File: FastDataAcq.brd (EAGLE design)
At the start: 114.3 x 63.2 mm, 223 parts, among them IC1 LT1963AEQ, IC2 FT230XQ, IC3 ADCMP553BRMZ, J1 MICRO-FIT_3.0_2POS_RA_SMD, J2 USB_MICROAB_SMT, J3 HEADER_0.1"_10P_2R_SMT, X1 87832-14, X2 SMA-142-0701-801/806, X3 SMA-142-0701-801/806, Y1 SI530-500, Y2 100MHz, Y3 DNP

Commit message: Digital layout complete.
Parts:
- moved TP13 25.2 mm to (76.4, 84.2)
- moved D2 17.0 mm to (106.7, 69.3), turned to 0 degrees
- moved R42 17.0 mm to (104.6, 69.3), flipped to the bottom, turned to 180 degrees
- moved D3 16.8 mm to (106.7, 67.8), turned to 0 degrees
- moved R43 16.8 mm to (104.6, 67.8), flipped to the bottom, turned to 180 degrees
- moved D4 11.7 mm to (106.7, 70.9), turned to 0 degrees
- moved R44 11.7 mm to (104.6, 70.9), flipped to the bottom, turned to 180 degrees
- moved J3 0.57 mm to (98.6, 73.4)
- moved Y3 0.28 mm to (84.3, 53.0)
- moved C85 0.25 mm to (88.4, 52.1)
- moved C86 0.25 mm to (87.4, 52.1)
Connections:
- removed net N3: U$2.P$62
- removed net N4: U$2.P$61
- removed net N5: U$2.P$59
- removed net N6: U$2.P$58
- removed net N7: U$2.P$57
- removed net N8: U$2.P$48
- removed net N9: U$2.P$47
- net 3V3: now also J3.P$9; no longer J3.P$1
- net FPGA_GPIO1: now also J3.P$4, U$2.P$47; no longer J3.P$9
- net FPGA_GPIO2: now also J3.P$2, U$2.P$48; no longer J3.P$8
- net FPGA_GPIO3: now also J3.P$1, U$2.P$57; no longer J3.P$7
- net FPGA_GPIO4: now also D3.CATHODE, J3.P$7, U$2.P$58; no longer J3.P$6
- net FPGA_GPIO5: now also J3.P$6, U$2.P$59; no longer J3.P$5
- net FPGA_GPIO6: now also D2.CATHODE, J3.P$5, U$2.P$61; no longer D3.CATHODE, J3.P$4
- net FPGA_GPIO7: now also U$2.P$62; no longer D2.CATHODE
- net GND: now also J3.P$10; no longer J3.P$2
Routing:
- net FPGA_GPIO1: track 0.00 -> 59.0 mm, vias 0 -> 2
- net FPGA_GPIO5: track 0.00 -> 57.6 mm, vias 0 -> 7
- net FPGA_GPIO2: track 0.00 -> 51.6 mm, vias 0 -> 2
- net FPGA_GPIO4: track 0.00 -> 48.7 mm, vias 0 -> 2
- net FPGA_GPIO6: track 0.00 -> 48.6 mm, vias 0 -> 4
- net FPGA_GPIO3: track 0.00 -> 42.2 mm, vias 0 -> 2
- net FPGA_GPIO7: track 0.00 -> 38.0 mm, vias 0 -> 2
- net 3V3: track 51.8 -> 83.8 mm, vias 27 -> 30
- net FPGA_TCK: track 38.4 -> 49.1 mm, vias 3 -> 4
- net FPGA_TMS: track 32.9 -> 42.8 mm, vias 3 -> 6
- net FPGA_TDI: track 30.1 -> 37.8 mm, vias 1 -> 2
- net GND: track 122.2 -> 128.4 mm, vias 140 -> 151
- net 1V8: track 49.6 -> 55.5 mm
- net PROM_TDO: track 6.54 -> 10.7 mm, vias 0 -> 2
- net N$22: track 0.00 -> 4.07 mm, vias 0 -> 1
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- added copper zone on layer 1, net 1V9
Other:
- board size 114.3 x 63.2 mm -> 114.3 x 62.7 mm

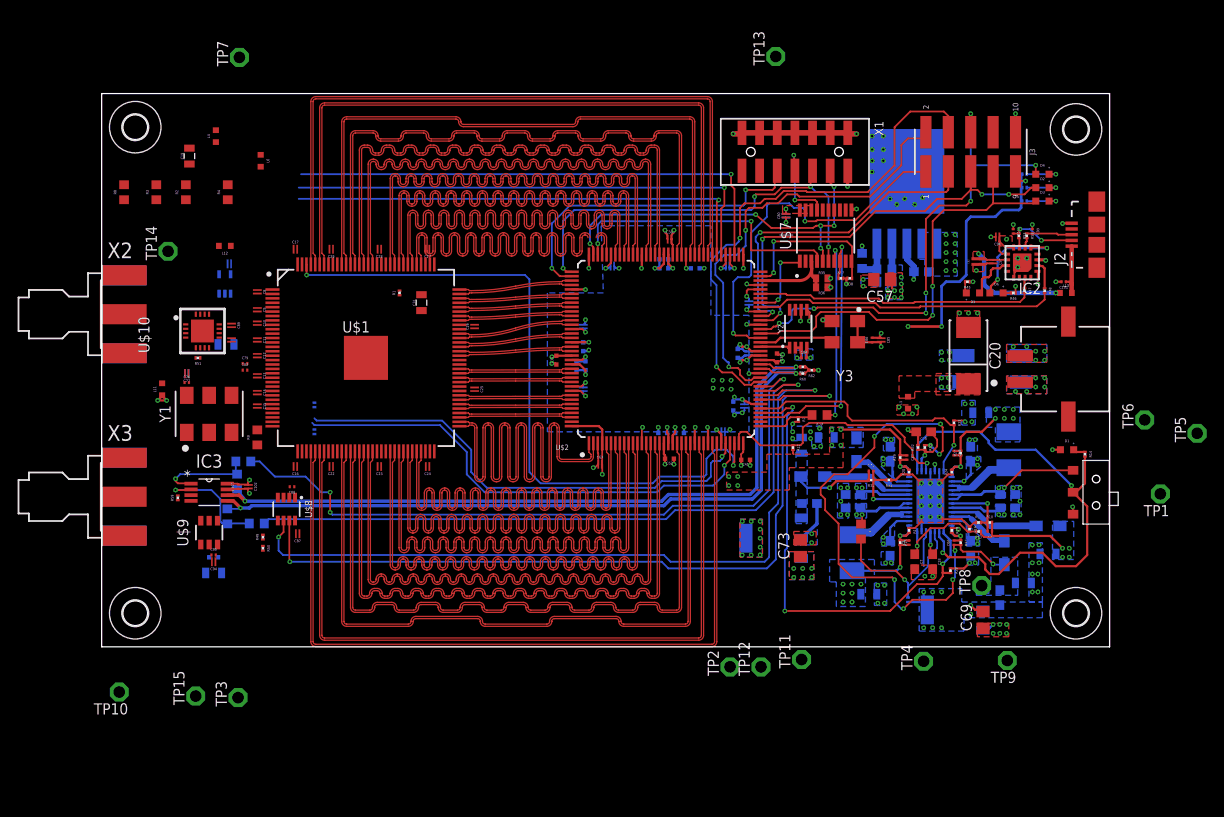
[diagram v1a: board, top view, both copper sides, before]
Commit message: PCB v0.1 done
Still need to fix a few things, but technically routing is done.
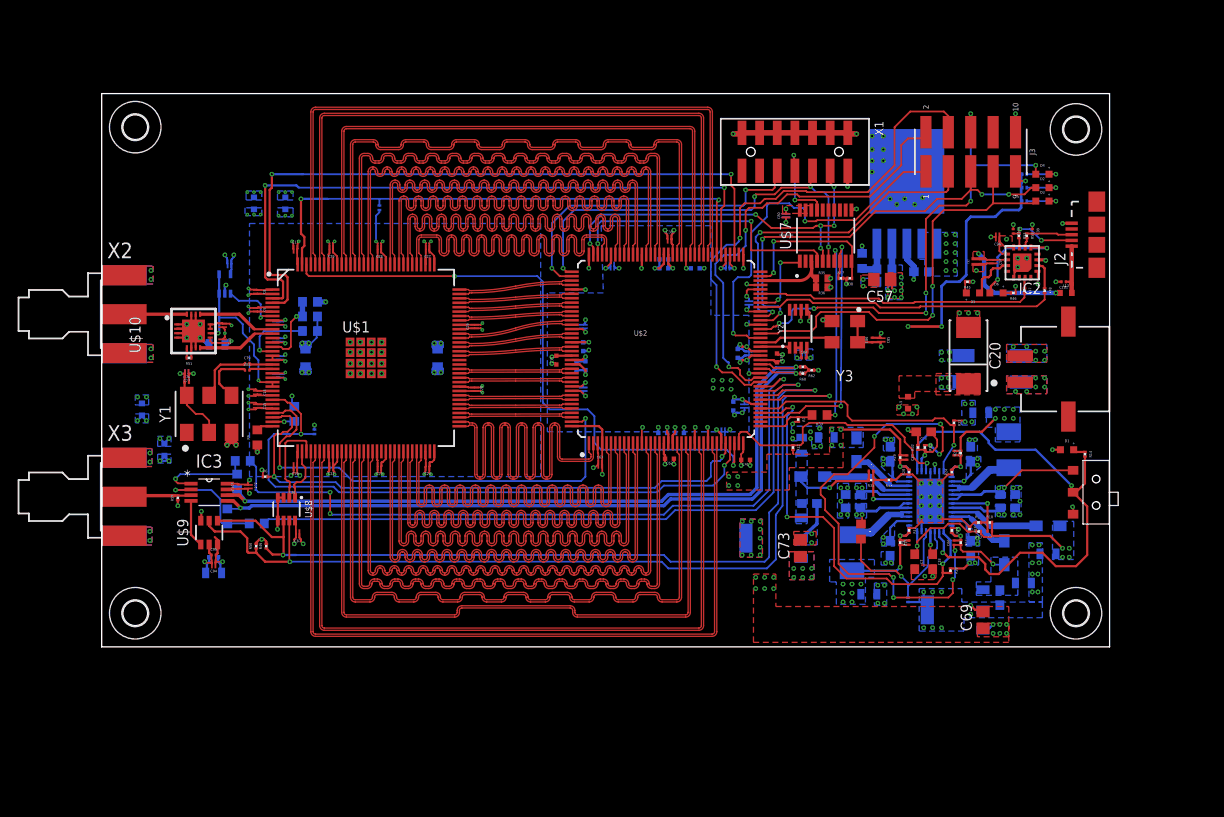
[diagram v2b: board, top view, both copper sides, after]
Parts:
- removed TP1, TP10, TP11, TP12, TP13, TP14, TP15, TP2, TP3, TP4, TP5, TP6, TP7, TP8, TP9: TPPAD1-13, testpad:P1-13
- moved R8 31.7 mm to (21.8, 43.7), flipped to the bottom
- moved C19 26.4 mm to (23.1, 50.0), flipped to the bottom
- moved R3 22.4 mm to (23.6, 54.7), flipped to the bottom, turned to 0 degrees
- moved L12 20.8 mm to (4.57, 44.2), flipped to the bottom, turned to 90 degrees
- moved R2 18.8 mm to (23.6, 56.4), flipped to the bottom, turned to 180 degrees
- moved R4 18.3 mm to (23.6, 53.1), flipped to the bottom, turned to 0 degrees
- moved R1 9.92 mm to (31.5, 67.1), flipped to the bottom, turned to 270 degrees
- moved R6 9.86 mm to (18.5, 36.6), flipped to the top, turned to 0 degrees
- moved L4 8.76 mm to (17.3, 67.6), flipped to the bottom
- moved L11 6.86 mm to (7.11, 39.6), flipped to the bottom
- moved C31 6.53 mm to (38.1, 50.0), flipped to the bottom
- moved L6 5.58 mm to (20.8, 67.6), flipped to the bottom, turned to 90 degrees
- moved C12 2.17 mm to (19.8, 50.0), flipped to the bottom
- moved C10 2.16 mm to (19.8, 54.0), flipped to the bottom
- moved C11 2.16 mm to (19.8, 52.1), flipped to the bottom
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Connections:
- net 1V2: no longer TP1.TP
- net 1V8: no longer TP5.TP
- net 1V9: no longer TP7.TP
- net 1V9A: no longer R1.2, R2.2
- net 1V9D: now also R1.2, R2.2
- net 2V3_1V9PRE: no longer TP6.TP
- net 2V5: no longer TP9.TP
- net 2V8_2V5PRE: no longer TP8.TP
- net 3V3: no longer TP3.TP
- net 3V3A: no longer TP10.TP
- net 3V3S: no longer TP14.TP
- net 3V6_PRE3V3: no longer TP11.TP
- net FPGA_DONE: no longer TP13.TP
- net FPGA_INITB: no longer TP12.TP
- net GND: now also U$1.P$130, U$1.P$131, U$1.P$132, U$1.P$133, U$1.P$134, U$1.P$135, U$1.P$136, U$1.P$137, U$1.P$138, U$1.P$139, U$1.P$140, U$1.P$141, U$1.P$142, U$1.P$143, U$1.P$144
- net PGOOD: no longer TP2.TP
- net S_TEMP: no longer TP4.TP
- net TRIG_REF: no longer TP15.TP
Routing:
- net GND: track 128.4 -> 226.0 mm, vias 151 -> 213
- net ADC_PDQ: track 0.00 -> 53.8 mm, vias 0 -> 2
- net 1V9A: track 0.00 -> 33.3 mm, vias 0 -> 18
- net 1V9D: track 0.00 -> 29.4 mm, vias 0 -> 14
- net ADC_OUTEDGE/DDR/SDATA: track 58.0 -> 79.5 mm, vias 1 -> 2
- net ADC_VCMO_BUFFER: track 0.00 -> 20.0 mm, vias 0 -> 2
- net ADC_OUTV/SCLK: track 56.0 -> 75.6 mm, vias 1 -> 2
- net ADC_PD: track 56.1 -> 73.1 mm, vias 1 -> 2
- net 3V3: track 83.8 -> 96.9 mm, vias 30 -> 33
- net FPGA_SCL: track 92.4 -> 105.2 mm
- net ADC_CAL: track 55.1 -> 66.7 mm, vias 1 -> 2
- net 2V5A: track 0.00 -> 10.9 mm, vias 0 -> 3
- net ADC_TDIODE-: track 0.00 -> 10.1 mm
- net FPGA_SDA: track 89.4 -> 99.5 mm
- net 3V3S: track 0.00 -> 9.36 mm, vias 0 -> 5
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- added copper zone on layer 16, net 1V9A
- added copper zone on layer 16, net 1V9D
- added copper zone on layer 16, net 2V5
- added copper zone on layer 16, net 2V5A
- added copper zone on layer 3, net 2V5A
- added copper zone on layer 16, net 3V3S
- added copper zone on layer 3, net 3V3S
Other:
- board text removed: "Check footprint for IC3"

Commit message: Several changes
There are several changes after discussing the design with Grant
Elliott. Most notably is the addition of a On/Off Debounce Latch IC.
Additionally the CTS is now connected to the FPGA to force the packet to
be sent.
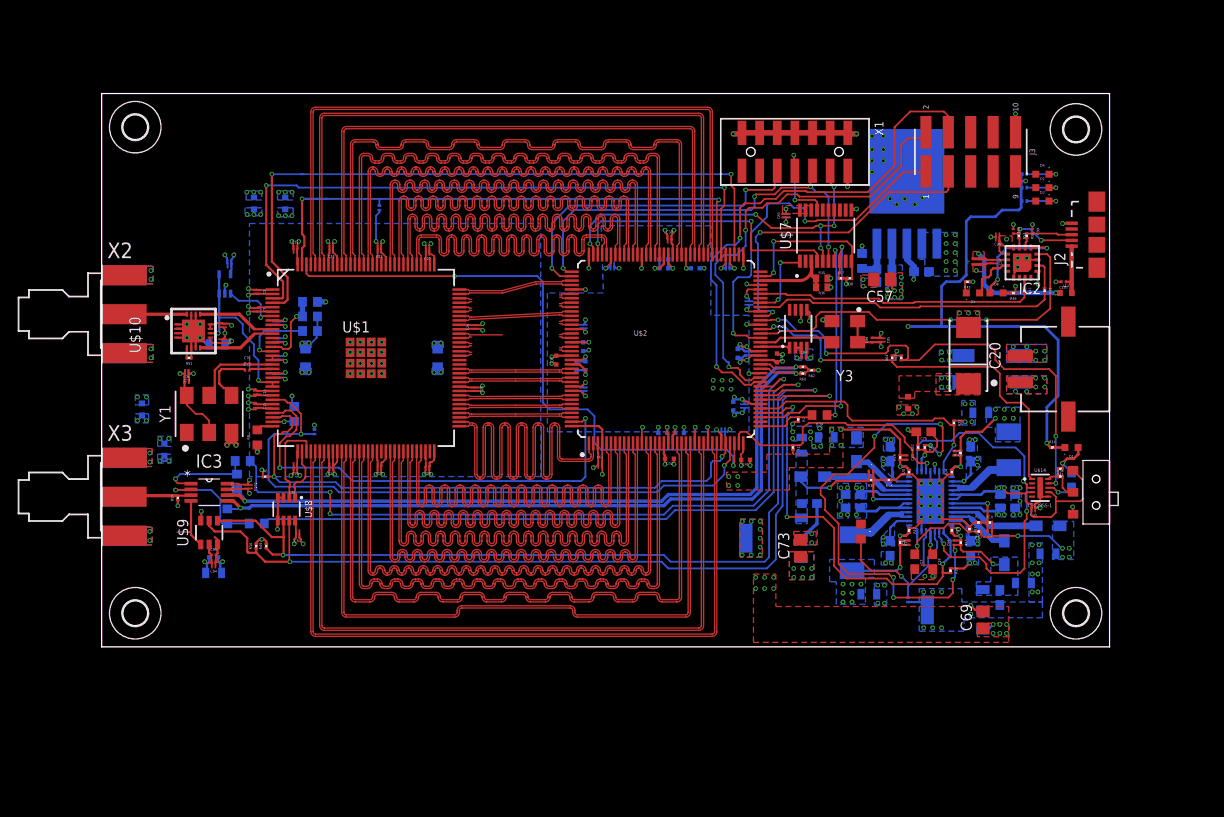
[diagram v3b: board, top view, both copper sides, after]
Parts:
- added C105: DNP, rcl:C0603
- added C30: .1uF, Schuyler:0204REVERSE
- added R34, R63, R64: 523K, rcl:R0201
- added R41: 113k, rcl:R0201
- added U$14: LTC2955-1, Schuyler:10-DFN
- R14: value 1k -> 330
- moved R14 3.76 mm to (107.8, 39.9), turned to 0 degrees
- moved D1 0.57 mm to (110.0, 39.9), turned to 180 degrees
- moved C27 0.25 mm to (37.0, 62.1)
- moved C26 0.06 mm to (42.3, 53.5)
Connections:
- removed net FPGA_GPIO4: D3.CATHODE, J3.P$7, U$2.P$58
- removed net FPGA_GPIO5: D4.CATHODE, J3.P$6, U$2.P$59
- removed net FPGA_GPIO6: D2.CATHODE, J3.P$5, U$2.P$61
- removed net N$9: D1.ANODE, R14.1
- new net !PB: U$14.P$5
- new net FPGA_CTS: D3.CATHODE, IC2.4, U$2.P$58
- new net N$1: D1.ANODE, R14.2
- new net N$12: R34.1, R41.2, U$14.P$10
- new net N$17: C105.1, U$14.P$8
- new net N$6: R34.2, S1.P$2
- new net PWR_INT: R64.1, U$14.P$1, U$2.P$59
- new net PWR_KILL: R63.1, U$14.P$9, U$2.P$61
- net 3V3: now also R14.1, R63.2, R64.2
- net GND: now also C105.2, C30.P$2, R41.1, U$14.P$11, U$14.P$6
- net PWR_ENABLE: now also U$14.P$3; no longer R14.2, S1.P$2
- net VIN: now also C30.P$1, U$14.P$4, U$14.P$7
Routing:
- net FPGA_GPIO5: track 57.6 -> 0.00 mm, vias 7 -> 0
- net PWR_KILL: track 0.00 -> 55.4 mm, vias 0 -> 4
- net FPGA_GPIO4: track 48.7 -> 0.00 mm, vias 2 -> 0
- net FPGA_GPIO6: track 48.6 -> 0.00 mm, vias 4 -> 0
- net PWR_INT: track 0.00 -> 45.5 mm, vias 0 -> 2
- net FPGA_CTS: track 0.00 -> 42.8 mm, vias 0 -> 2
- net 3V3: track 96.9 -> 125.5 mm, vias 33 -> 34
- net PWR_ENABLE: track 59.8 -> 44.6 mm, vias 2 -> 3
- net DI6-: track 13.0 -> 2.88 mm
- net DI7-: track 12.9 -> 2.89 mm
- net DI7+: track 12.9 -> 2.89 mm
- net DI4+: track 12.9 -> 2.88 mm
- net ADC_DCLK+: track 12.9 -> 2.88 mm
- net DI3-: track 12.9 -> 2.89 mm
- net DI3+: track 12.9 -> 2.89 mm
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
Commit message: PCB Power Layer and Other Fixes
Finalized the FPGA GPIO Pins. Fixed power layer so that all spacing is
equal and entire layer covered. Other cosmetic fixes.
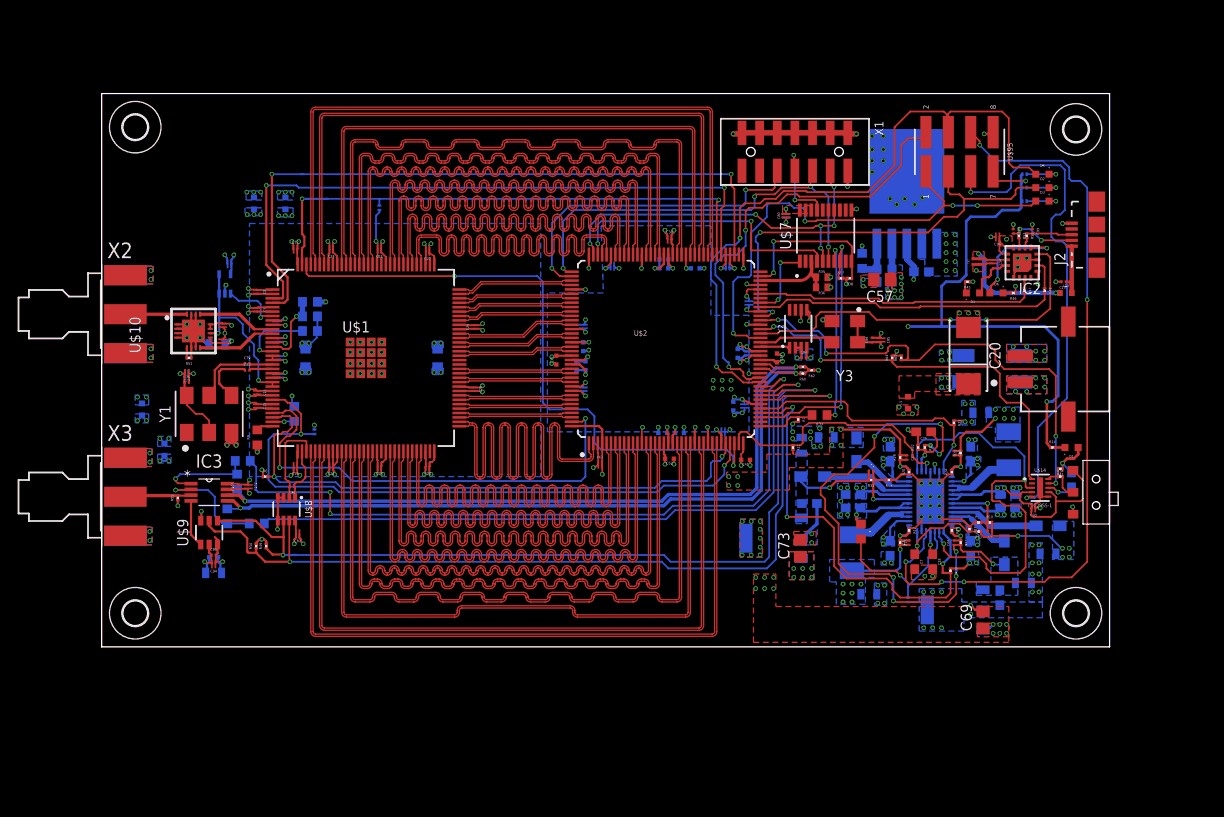
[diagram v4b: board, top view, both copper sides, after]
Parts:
- removed J3: HEADER_0.1"_10P_2R_SMT, Schuyler:HEADER_10P_2R_SMT
- added U$95: HEADER_0.1"_8P_2R_SMT, Schuyler:HEADER_8P_2R_SMT
- R2, R3, R4, R8: value NA -> DNP
- R40: value 0 -> DNP
- moved R35 0.13 mm to (81.7, 59.2)
- moved C25 0.13 mm to (42.2, 46.5)
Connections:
- net ADC_DCLK+ renamed ADC_DCLK_P
- net ADC_DCLK- renamed ADC_DCLK_N
- net DI2+ renamed DI2_P
- net DI2- renamed DI2_N
- net DI3+ renamed DI3_P
- net DI3- renamed DI3_N
- net DI4+ renamed DI4_P
- net DI4- renamed DI4_N
- net DI5+ renamed DI5_P
- net DI5- renamed DI5_N
- net DI6+ renamed DI6_P
- net DI6- renamed DI6_N
- net DI7+ renamed DI7_P
- net DI7- renamed DI7_N
- net DQ3+ renamed DQ3_N
- net DQ3- renamed DQ3_P
- net DQ4+ renamed DQ4_N
- net DQ4- renamed DQ4_P
- net DQ5+ renamed DQ5_N
- net DQ5- renamed DQ5_P
- net DQ6+ renamed DQ6_N
- net DQ6- renamed DQ6_P
- net DQ7+ renamed DQ7_N
- net DQ7- renamed DQ7_P
- removed net FPGA_GPIO7: J3.P$3, U$2.P$62
- new net FPGA_GPIO4: D2.CATHODE, U$2.P$62, U$95.P$3
- net !PB: now also U$95.P$5
- net 3V3: now also U$95.P$7; no longer J3.P$9
- net FPGA_CTS: no longer D3.CATHODE
- net FPGA_GPIO1: now also D4.CATHODE, U$95.P$4; no longer J3.P$4
- net FPGA_GPIO2: now also U$95.P$2; no longer J3.P$2
- net FPGA_GPIO3: now also D3.CATHODE, U$95.P$1; no longer J3.P$1
- net GND: now also U$95.P$8; no longer J3.P$10
- net S_TEMP: now also U$95.P$6
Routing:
- net S_TEMP: track 4.07 -> 87.9 mm, vias 0 -> 5
- net !PB: track 0.00 -> 57.8 mm, vias 0 -> 2
- net FPGA_GPIO4: track 0.00 -> 51.4 mm, vias 0 -> 2
- net FPGA_GPIO7: track 38.0 -> 0.00 mm, vias 2 -> 0
- net FPGA_GPIO1: track 59.0 -> 74.9 mm
- net FPGA_GPIO3: track 42.2 -> 58.0 mm, vias 2 -> 4
- net DI6_N: track 2.88 -> 13.5 mm
- net DI7_N: track 2.89 -> 13.3 mm
- net DI7_P: track 2.89 -> 13.3 mm
- net DI4_P: track 2.88 -> 13.0 mm
- net ADC_DCLK_N: track 2.89 -> 13.1 mm
- net DI3_P: track 2.89 -> 13.1 mm
- net DI4_N: track 2.90 -> 13.1 mm
- net DI3_N: track 2.89 -> 13.0 mm
- net ADC_DCLK_P: track 2.88 -> 13.0 mm
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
